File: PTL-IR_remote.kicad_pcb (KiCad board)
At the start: 2 copper layers, 25.4 x 37.9 mm, 15 parts, among them J1 8p, J2 8p, Q1 2N7002, U1 TSOP45xx

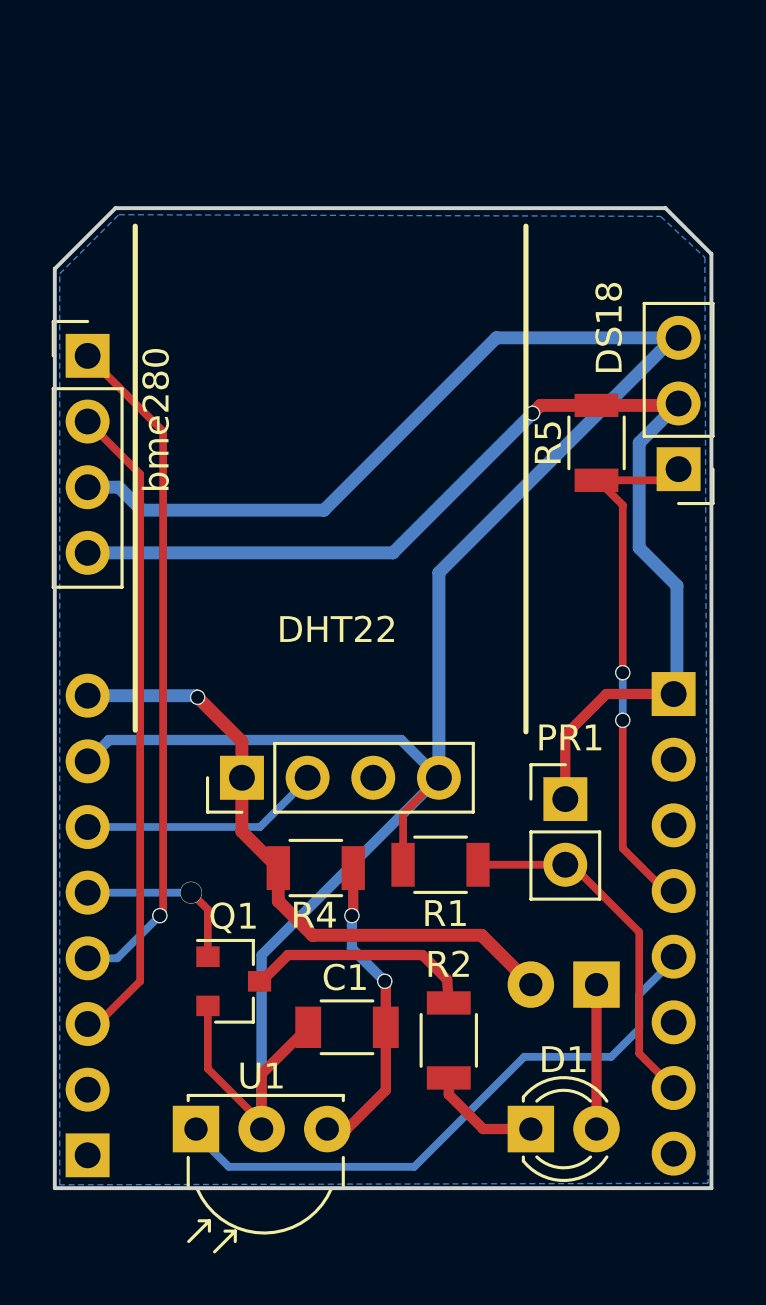
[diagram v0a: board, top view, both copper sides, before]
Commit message: fix pcb v1.0 (and update to kicad v5)
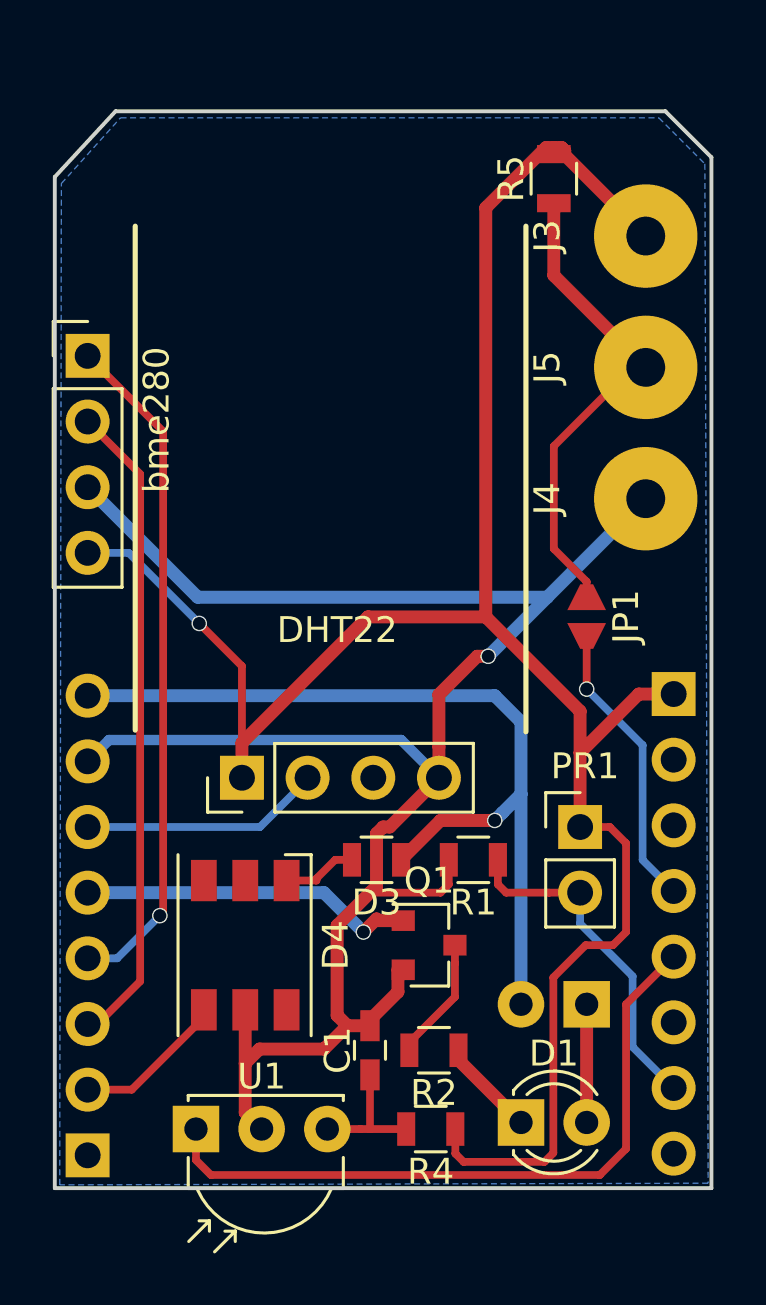
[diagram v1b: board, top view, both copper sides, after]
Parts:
- removed DS18: DS18, Socket_Strips:Socket_Strip_Straight_1x03_Pitch2.54mm
- added D3: DIODE, Resistors_SMD:R_0805, F.Cu at (185.2, 106.7)
- added D4: WS2813, LEDs:LED_WS2812-PLCC6, F.Cu at (180.1, 110.0)
- added J3: Pad, Wire_Pads:SolderWirePad_single_1-5mmDrill, F.Cu at (195.6, 82.5)
- added J4: Pad, Wire_Pads:SolderWirePad_single_1-5mmDrill, F.Cu at (195.6, 92.7)
- added J5: Pad, Wire_Pads:SolderWirePad_single_1-5mmDrill, F.Cu at (195.6, 87.6)
- added JP1: Jumper, PTL-ino:solder-jumper-2, F.Cu at (193.3, 97.3)
- C1: footprint Capacitors_SMD:C_1206 -> Capacitors_SMD:C_0603_HandSoldering
- PR1: value PHOTO -> PHOTO (1MΩ)
- R1: value 1kΩ -> 1kΩ (10kΩ); footprint Resistors_SMD:R_1206 -> Resistors_SMD:R_0805
- R2, R4, R5: footprint Resistors_SMD:R_1206 -> Resistors_SMD:R_0805
- moved R4 11.0 mm to (187.3, 117.1), turned to 180 degrees
- moved R5 10.4 mm to (192.0, 80.3)
- moved Q1 7.68 mm to (187.2, 110.0)
- moved R1 1.28 mm to (188.9, 106.7)
- moved C1 1.26 mm to (184.9, 114.0), turned to 90 degrees
- moved PR1 1.22 mm to (193.0, 105.4)
- moved D2 0.85 mm to (193.3, 112.3)
- moved R2 0.69 mm to (187.4, 114.0), turned to 180 degrees
- moved D1 0.46 mm to (190.8, 116.8)
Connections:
- DHT22 pad 1: +5V -> +3V3
- DHT22 pad 3: (no net) -> Net-(DHT22-Pad3)
- J1 pad 2: (no net) -> Net-(J1-Pad2)
- J1 pad 3: (no net) -> Net-(J1-Pad3)
- J1 pad 6: (no net) -> Net-(J1-Pad6)
- J1 pad 8: (no net) -> Net-(J1-Pad8)
- J2 pad 1: (no net) -> Net-(J2-Pad1)
- J2 pad 2: (no net) -> /RX
- R4 pad 1: +5V -> +3V3
- R5 pad 1: /D6 -> Net-(J5-Pad1)
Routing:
- net +3V3: track 44.9 -> 84.4 mm
- net Net-(J5-Pad1): track 0.00 -> 18.5 mm
- net GND: track 92.3 -> 77.2 mm, vias 0 -> 1
- net /D6: track 20.8 -> 11.3 mm, vias 2 -> 1
- net +5V: track 24.6 -> 33.8 mm
- net Net-(C1-Pad1): track 12.5 -> 5.34 mm, vias 2 -> 0
- net Net-(J2-Pad5): track 6.75 -> 13.1 mm
- net /RX: track 0.00 -> 5.95 mm
- net Net-(Q1-Pad3): track 9.18 -> 4.79 mm
- net /D5: track 23.5 -> 26.7 mm
- net Net-(D3-Pad2): track 0.00 -> 2.91 mm
- net Net-(D1-Pad1): track 5.03 -> 3.80 mm
- net Net-(D1-Pad2): track 5.59 -> 4.57 mm
- net /ADC: track 14.0 -> 13.3 mm
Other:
- board size 25.4 x 37.9 mm -> 25.4 x 41.7 mm

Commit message: split schema
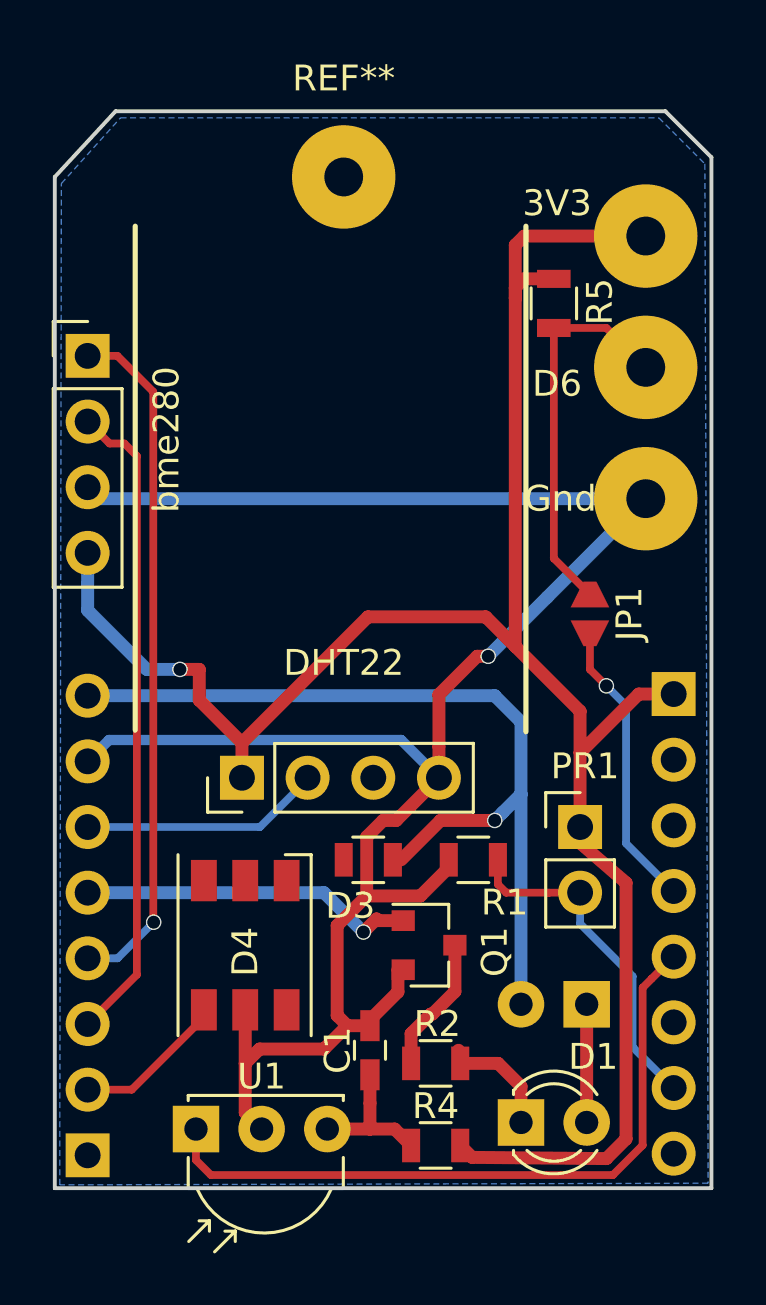
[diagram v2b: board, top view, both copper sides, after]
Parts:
- removed J5: Pad, Wire_Pads:SolderWirePad_single_1-5mmDrill
- added ?: , PTL-ino:PTL_mini, B.Cu at (192.5, 89.2)
- added D6: Pad, Wire_Pads:SolderWirePad_single_1-5mmDrill, F.Cu at (195.6, 87.6)
- added G***: LOGO, PTL-ino:Logo_silk_CC-BY-SA_10x4.5mm, B.Cu at (182.6, 112.8)
- added REF**: SolderWirePad_single_1-5mmDrill, Wire_Pads:SolderWirePad_single_1-5mmDrill, F.Cu at (183.9, 80.3)
- moved R5 4.83 mm to (192.0, 85.2)
- moved R4 0.66 mm to (187.5, 117.7)
- moved R2 0.51 mm to (187.5, 114.6)
- moved D3 0.32 mm to (184.8, 106.7)
- moved JP1 0.16 mm to (193.4, 97.2)
- renumbered J3 to 3V3, J4 to Gnd
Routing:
- net +3V3: track 84.4 -> 80.9 mm
- net Net-(J5-Pad1): track 18.5 -> 15.1 mm
- net Net-(D3-Pad2): track 2.91 -> 0.00 mm
- net GND: track 77.2 -> 79.4 mm
- net Net-(D1-Pad1): track 3.80 -> 4.49 mm
- net Net-(Q1-Pad3): track 4.79 -> 5.31 mm
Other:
- board text added: "3V3"
- board text added: "5V"
- board text added: "A0"
- board text added: "D4"
- board text added: "G"
- board text added: "LemanMake 18"
- board text added: "v1.1"
- board text removed: "LemanMake 2018"
- board text removed: "v1.0"

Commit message: minor changes
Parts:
- removed REF**: SolderWirePad_single_1-5mmDrill, Wire_Pads:SolderWirePad_single_1-5mmDrill
- added screw: SolderWirePad_single_1-5mmDrill, Wire_Pads:SolderWirePad_single_1-5mmDrill, F.Cu at (183.9, 80.3)
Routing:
- net Net-(D3-Pad2): track 0.00 -> 2.54 mm
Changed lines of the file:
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@@
     (thickness 1.6)
     (drawings 20)
-    (tracks 140)
+    (tracks 142)
     (zones 0)
     (modules 23)
@@
   )
   (page A4)
+  (title_block
+    (title "PTL IR remote ")
+    (date 2018-07-28)
+    (rev v1.1)
+    (company "Post Tenebras Lab")
+    (comment 1 "Atelier LemanMake 2018")
+  )
   (layers
     (0 F.Cu signal)
-    (31 B.Cu signal hide)
+    (31 B.Cu signal)
     (32 B.Adhes user)
     (33 F.Adhes user)
@@
     (46 B.CrtYd user)
     (47 F.CrtYd user)
-    (48 B.Fab user hide)
+    (48 B.Fab user)
     (49 F.Fab user)
   )
   (setup
-    (last_trace_width 0.5)
+    (last_trace_width 0.4)
     (user_trace_width 0.3)
     (user_trace_width 0.5)
@@
     (visible_elements FFFFFF7F)
     (pcbplotparams
-      (layerselection 0x00830_80000001)
+      (layerselection 0x018f0_ffffffff)
       (usegerberextensions false)
       (usegerberattributes false)
@@
       (drillshape 0)
       (scaleselection 1)
-      (outputdirectory "/home/seba/projects/PostTenebrasLab/PTL-ir_remote/"))
+      (outputdirectory "gerber/"))
   )
   (net 0 "")
@@
   (module Wire_Pads:SolderWirePad_single_1-5mmDrill (layer F.Cu)
     (at 183.896 80.264)
-    (fp_text reference REF** (at 0 -3.81) (layer F.SilkS)
+    (fp_text reference screw (at 0 2.921 180) (layer F.SilkS)
       (effects (font (size 1 1) (thickness 0.15)))
     )
@@
   (segment (start 194.056 86.106) (end 195.58 87.63) (width 0.3) (layer F.Cu) (net 22))
   (segment (start 192.024 86.106) (end 194.056 86.106) (width 0.3) (layer F.Cu) (net 22))
+  (segment (start 183.094 107.482) (end 183.896 106.68) (width 0.5) (layer F.Cu) (net 23))
+  (segment (start 181.686 107.482) (end 183.094 107.482) (width 0.5) (layer F.Cu) (net 23))
   (zone (net 5) (net_name GND) (layer B.Cu) (hatch edge 0.508)
     (connect_pads (clearance 0.508))

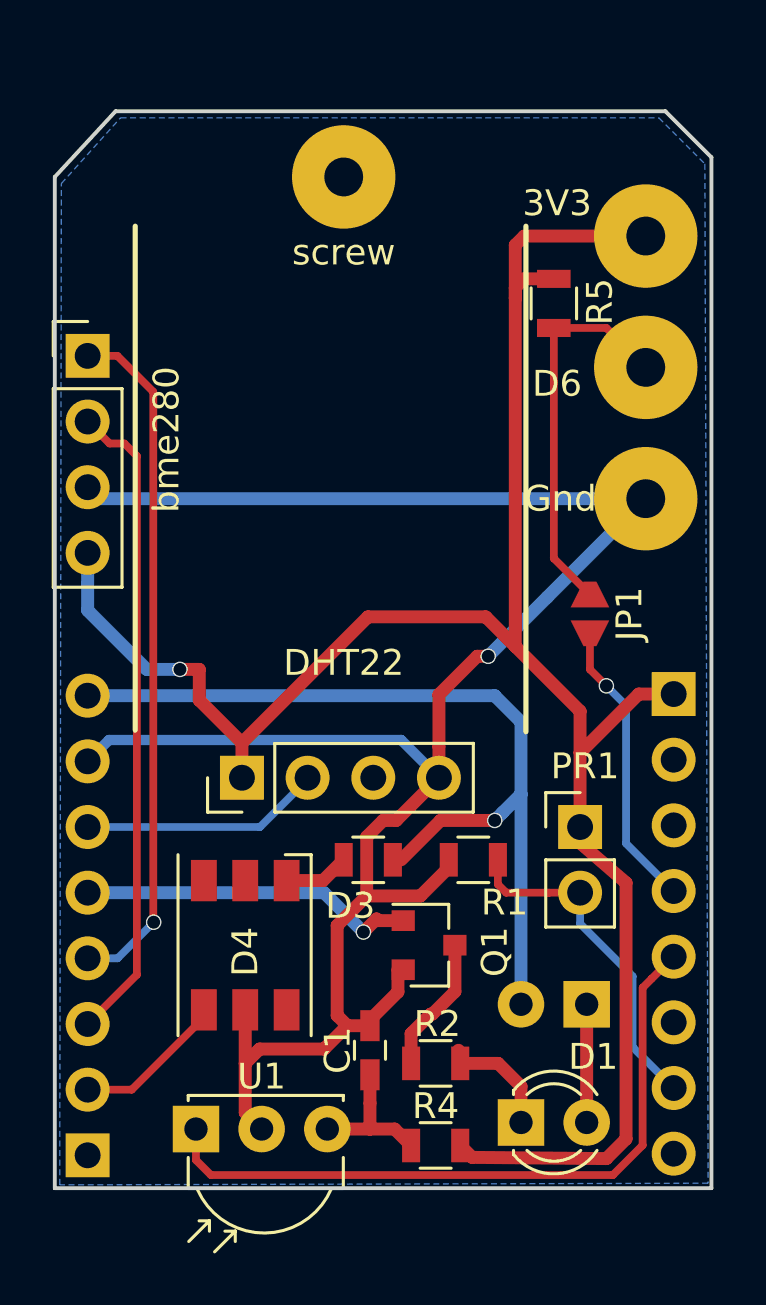
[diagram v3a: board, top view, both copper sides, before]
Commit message: change diode footprint and reroute
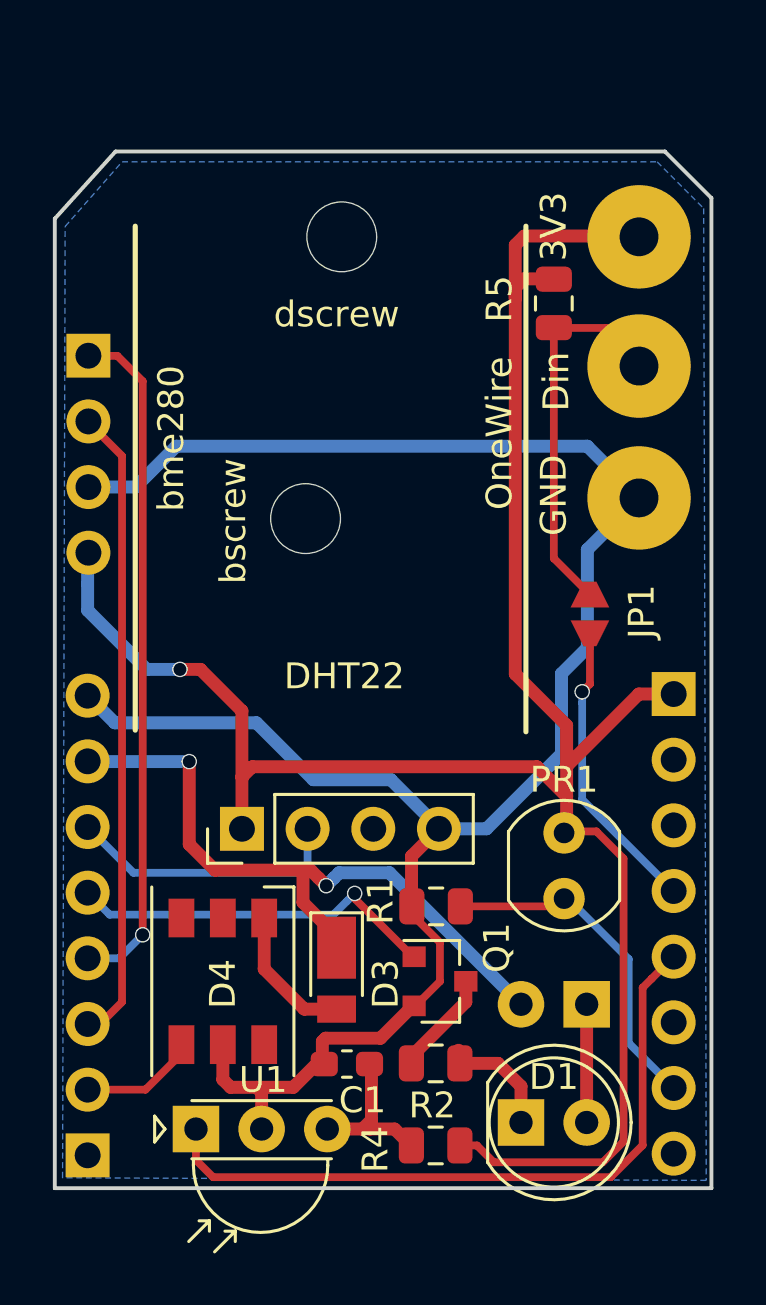
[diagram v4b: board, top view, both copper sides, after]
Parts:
- removed D6, Gnd: Pad, Wire_Pads:SolderWirePad_single_1-5mmDrill
- removed bme280: bme280, Pin_Headers:Pin_Header_Straight_1x04_Pitch2.54mm
- removed screw: SolderWirePad_single_1-5mmDrill, Wire_Pads:SolderWirePad_single_1-5mmDrill
- added Din: Pad, Connector_Wire:SolderWirePad_1x01_Drill1.5mm, F.Cu at (195.3, 87.6)
- added GND: Pad, Connector_Wire:SolderWirePad_1x01_Drill1.5mm, F.Cu at (195.3, 92.7)
- added J3: bme280, Connector_PinHeader_2.54mm:PinHeader_1x04_P2.54mm_Vertical, B.Cu at (174.0, 87.2)
- added bscrew: MountingHole_2.7mm_M2.5, MountingHole:MountingHole_2.7mm_M2.5, F.Cu at (182.4, 93.5)
- added dscrew: MountingHole_2.7mm_M2.5, MountingHole:MountingHole_2.7mm_M2.5, F.Cu at (183.8, 82.6)
- 3V3: footprint Wire_Pads:SolderWirePad_single_1-5mmDrill -> Connector_Wire:SolderWirePad_1x01_Drill1.5mm
- C1: footprint Capacitors_SMD:C_0603_HandSoldering -> Capacitor_SMD:C_0603_1608Metric_Pad1.05x0.95mm_HandSolder
- D1, D2: footprint LEDs:LED_D3.0mm -> LED_THT:LED_D5.0mm_IRGrey
- D3: footprint Resistors_SMD:R_0805 -> Diode_SMD:D_PowerDI-123
- D4: footprint LEDs:LED_WS2812-PLCC6 -> LED_SMD:LED_WS2812_PLCC6_5.0x5.0mm_P1.6mm
- DHT22: footprint Socket_Strips:Socket_Strip_Straight_1x04_Pitch2.54mm -> Connector_PinHeader_2.54mm:PinHeader_1x04_P2.54mm_Vertical
- J1, J2: footprint Socket_Strips:Socket_Strip_Straight_1x08_Pitch2.54mm -> Connector_PinHeader_2.54mm:PinHeader_1x08_P2.54mm_Vertical
- PR1: footprint Socket_Strips:Socket_Strip_Straight_1x02_Pitch2.54mm -> OptoDevice:R_LDR_4.9x4.2mm_P2.54mm_Vertical
- Q1: footprint TO_SOT_Packages_SMD:SOT-23 -> Package_TO_SOT_SMD:SOT-23
- R1, R2, R4, R5: footprint Resistors_SMD:R_0805 -> Resistor_SMD:R_0805_2012Metric
- U1: value TSOP45xx -> TSOP4838; footprint Opto-Devices:IRReceiver_Vishay_MOLD-3pin -> OptoDevice:Vishay_MINIMOLD-3Pin
- moved ? 5.18 mm to (191.8, 94.3)
- moved D3 4.42 mm to (183.6, 110.9), turned to 270 degrees
- moved R1 2.31 mm to (187.5, 108.5)
- moved DHT22 1.98 mm to (180.0, 105.5)
- moved D4 1.64 mm to (179.2, 111.4)
- moved Q1 1.46 mm to (187.6, 111.4)
- moved C1 1.04 mm to (184.0, 114.6), turned to 180 degrees
- moved G*** 0.81 mm to (181.8, 112.9)
- moved PR1 0.66 mm to (192.4, 105.6), turned to 270 degrees
- moved 3V3 0.26 mm to (195.3, 82.6)
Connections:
- net /ADC renamed PhR
- net /D4 renamed DHT
- net /D5 renamed IRM
- net /D6 renamed OneW
- net /RX renamed RGB
- net Net-(J2-Pad5) renamed IR
- C1 pad 2: GND -> GNDREF
- D4 pad 5: GND -> GNDREF
- DHT22 pad 4: GND -> GNDREF
- J2 pad 3: /SCL -> SCL
- J2 pad 4: /SDA -> SDA
- J2 pad 7: GND -> +5V
- J2 pad 8: +5V -> GNDREF
- Q1 pad 2: GND -> GNDREF
- R1 pad 2: GND -> GNDREF
- U1 pad 2: GND -> GNDREF
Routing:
- net GND: track 79.4 -> 0.00 mm, vias 1 -> 0
- net GNDREF: track 0.00 -> 76.1 mm
- net /SDA: track 26.8 -> 0.00 mm, vias 1 -> 0
- net SDA: track 0.00 -> 26.5 mm, vias 0 -> 1
- net /SCL: track 26.2 -> 0.00 mm
- net SCL: track 0.00 -> 25.6 mm
- net +5V: track 33.8 -> 26.5 mm, vias 1 -> 2
- net +3V3: track 80.9 -> 84.8 mm
- net Net-(D3-Pad2): track 2.54 -> 5.47 mm
- net DHT: track 9.34 -> 11.4 mm
- net RGB: track 5.95 -> 4.51 mm
- net IR: track 13.1 -> 14.5 mm
- net Net-(Q1-Pad3): track 5.31 -> 4.05 mm
- net Net-(C1-Pad1): track 5.79 -> 6.35 mm
- added copper zone on B.Cu, net GNDREF
- removed copper zone on B.Cu, net GND
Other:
- board size 25.4 x 41.7 mm -> 25.4 x 40.1 mm
- board text added: "OneWire"
- board text added: "bme280"

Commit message: change led pin (D2), add jumper (bme280)
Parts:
- moved JP1 21.4 mm to (176.3, 84.3), turned to 90 degrees
- moved R5 4.59 mm to (191.9, 89.7)
- moved 3V3 3.30 mm to (195.3, 85.9)
- moved D 3.10 mm to (195.3, 90.7)
- moved Gnd 2.80 mm to (195.3, 95.5)
- renumbered Din to D, GND to Gnd
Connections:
- D pad 1: Net-(J5-Pad1) -> OneW
- D4 pad 2: Net-(D4-Pad2) -> (no net)
- D4 pad 3: Net-(D4-Pad3) -> (no net)
- D4 pad 4: RGB -> D2
- D4 pad 6: Net-(D4-Pad6) -> (no net)
- DHT22 pad 3: Net-(DHT22-Pad3) -> (no net)
- J1 pad 2: Net-(J1-Pad2) -> (no net)
- J1 pad 3: Net-(J1-Pad3) -> (no net)
- J1 pad 6: Net-(J1-Pad6) -> (no net)
- J1 pad 8: Net-(J1-Pad8) -> (no net)
- J2 pad 1: Net-(J2-Pad1) -> (no net)
- J2 pad 2: RGB -> (no net)
- J2 pad 3: SCL -> D2
- J3 pad 2: SCL -> /SCL
- JP1 pad 1: Net-(J5-Pad1) -> D2
- JP1 pad 2: OneW -> /SCL
- R5 pad 1: Net-(J5-Pad1) -> OneW
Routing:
- net D2: track 0.00 -> 32.4 mm
- net SCL: track 25.6 -> 0.00 mm
- net Net-(J5-Pad1): track 15.1 -> 0.00 mm
- net GNDREF: track 76.1 -> 62.6 mm
- net OneW: track 11.6 -> 22.6 mm
- net /SCL: track 0.00 -> 10.9 mm, vias 0 -> 1
- net +3V3: track 84.8 -> 77.4 mm
- net RGB: track 4.51 -> 0.00 mm
- net SDA: track 26.5 -> 24.7 mm, vias 1 -> 0
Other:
- outline, holes or cut-outs redrawn
- board text added: "I2C"
- board text removed: "bme280"

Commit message: replace OneWIre pads by 2.54 header
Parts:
- removed 3V3, D, Gnd: Pad, Connector_Wire:SolderWirePad_1x01_Drill1.5mm
- added J4: Conn_01x03_Female, Connector_PinHeader_2.54mm:PinHeader_1x03_P2.54mm_Vertical, F.Cu at (196.6, 94.8)
- moved JP1 21.4 mm to (176.9, 105.7)
- moved R5 4.05 mm to (194.8, 86.9), turned to 180 degrees
- moved PR1 3.06 mm to (193.6, 108.5), turned to 180 degrees
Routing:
- net D2: track 32.4 -> 11.1 mm
- net /SCL: track 10.9 -> 17.4 mm
- net +3V3: track 77.4 -> 72.1 mm, vias 1 -> 3
- net GNDREF: track 62.6 -> 64.5 mm
- net OneW: track 22.6 -> 23.1 mm
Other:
- board text added: "D6"
- board text added: "Gnd"
